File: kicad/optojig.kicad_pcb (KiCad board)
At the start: 2 copper layers, 200 x 100 mm, 20 parts, among them Q1 2N2219, Q2 2N2219, SW1 Switch_SPDT_x2, U1 TRN1-0510, U2 LM358

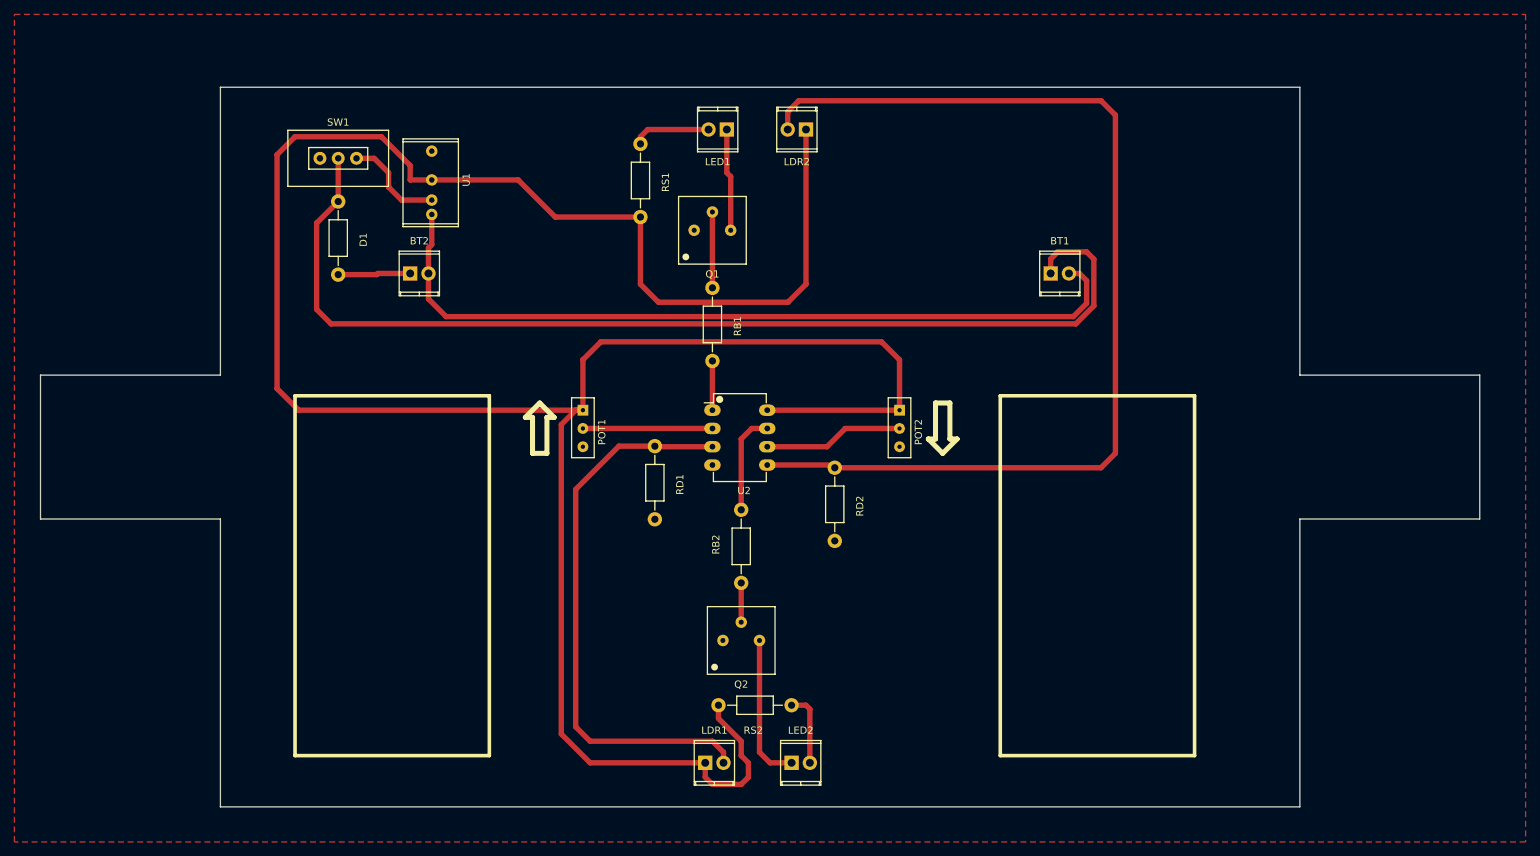
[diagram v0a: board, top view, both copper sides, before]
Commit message: Added battery holder datasheet
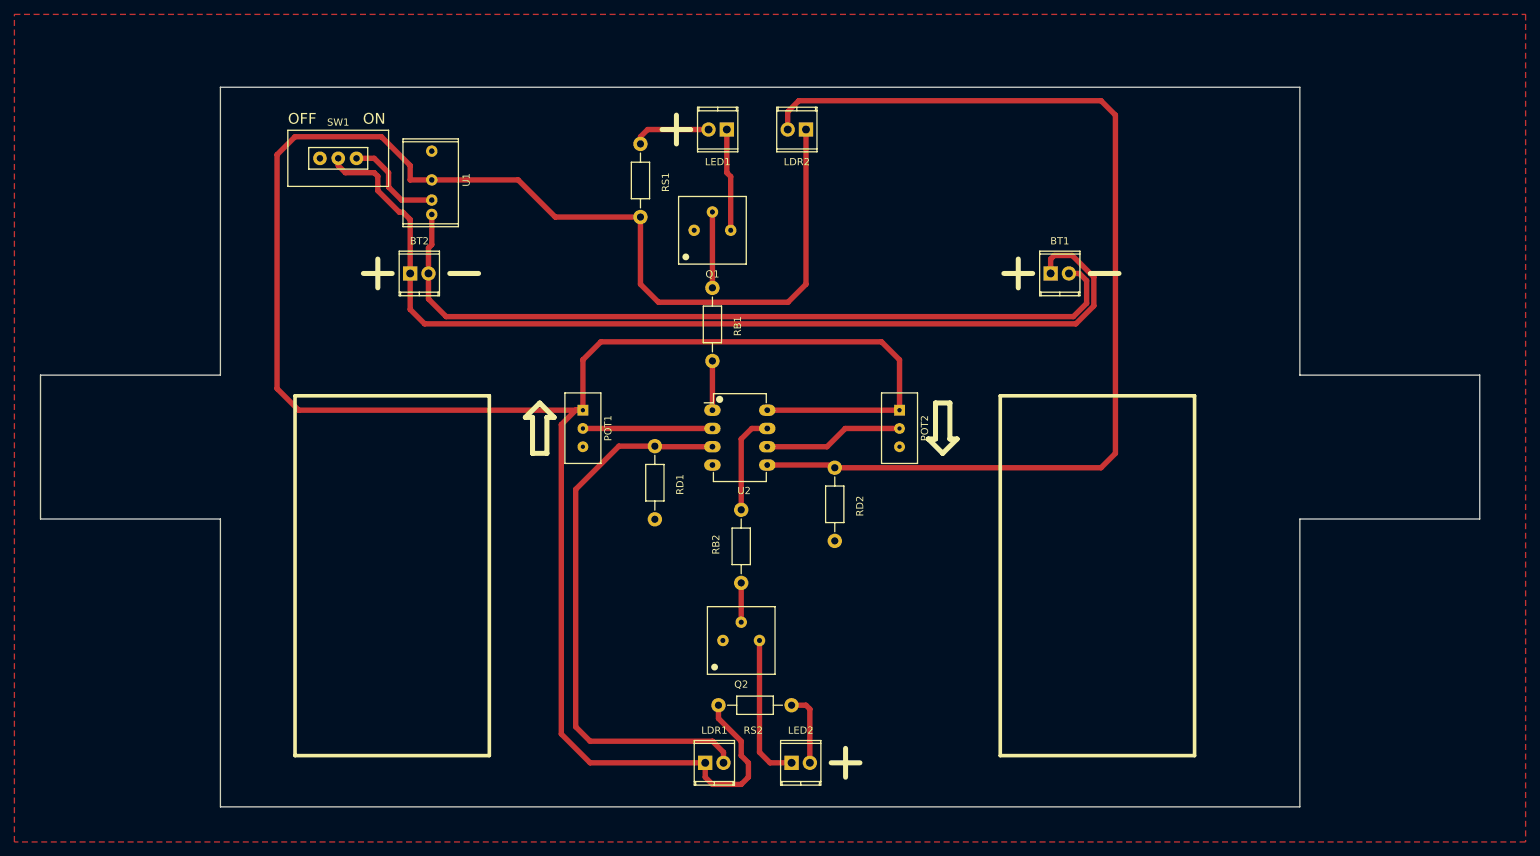
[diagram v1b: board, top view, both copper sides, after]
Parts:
- removed D1: D, Resistors_ThroughHole:Resistor_Horizontal_RM10mm
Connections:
- BT2 pad 1: Net-(BT2-Pad1) -> Net-(BT1-Pad1)
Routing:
- net Net-(BT2-Pad1): track 10.1 -> 0.00 mm
- net Net-(BT1-Pad1): track 147.4 -> 138.1 mm
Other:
- board text added: "OFF"
- board text added: "ON"

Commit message: Added final PCB version
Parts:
- added Battery 1: Batt_hold, optojig-footprints:Batt_hold, F.Cu at (92.8, 115.9)
- added Battery 2: Batt_hold, optojig-footprints:Batt_hold, F.Cu at (190.6, 116.0)
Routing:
- added copper zone on B.Cu, net GND
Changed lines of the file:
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@@
     (area 40 35 250.000001 150.000001)
     (thickness 1.6)
-    (drawings 46)
+    (drawings 38)
     (tracks 109)
     (zones 0)
-    (modules 19)
+    (modules 21)
     (nets 19)
   )
@@
   (layers
     (0 F.Cu signal)
-    (31 B.Cu signal)
-    (32 B.Adhes user)
-    (33 F.Adhes user)
-    (34 B.Paste user)
-    (35 F.Paste user)
-    (36 B.SilkS user)
+    (31 B.Cu signal hide)
+    (32 B.Adhes user hide)
+    (33 F.Adhes user hide)
+    (34 B.Paste user hide)
+    (35 F.Paste user hide)
+    (36 B.SilkS user hide)
     (37 F.SilkS user)
-    (38 B.Mask user)
-    (39 F.Mask user)
-    (40 Dwgs.User user)
-    (41 Cmts.User user)
-    (42 Eco1.User user)
-    (43 Eco2.User user)
-    (44 Edge.Cuts user)
-    (45 Margin user)
-    (46 B.CrtYd user)
-    (47 F.CrtYd user)
-    (48 B.Fab user)
-    (49 F.Fab user)
+    (38 B.Mask user hide)
+    (39 F.Mask user hide)
+    (40 Dwgs.User user hide)
+    (41 Cmts.User user hide)
+    (42 Eco1.User user hide)
+    (43 Eco2.User user hide)
+    (44 Edge.Cuts user hide)
+    (45 Margin user hide)
+    (46 B.CrtYd user hide)
+    (47 F.CrtYd user hide)
+    (48 B.Fab user hide)
+    (49 F.Fab user hide)
   )
   (setup
@@
     (visible_elements FFFFFF7F)
     (pcbplotparams
-      (layerselection 0x00030_80000001)
+      (layerselection 0x010e0_80000001)
       (usegerberextensions false)
       (excludeedgelayer true)
@@
       (outputformat 1)
       (mirror false)
-      (drillshape 1)
+      (drillshape 0)
       (scaleselection 1)
-      (outputdirectory ""))
+      (outputdirectory gerber/))
   )
   (net 0 "")
@@
     (add_net "Net-(SW1-Pad3)")
   )
+  (module optojig-footprints:Batt_hold (layer F.Cu)
+    (at 190.63 115.95)
+    (fp_text reference "Battery 2" (at 0.25 26.05) (layer F.SilkS)
+      (effects (font (size 1 1) (thickness 0.15)))
+    )
+    (fp_text value Batt_hold (at 0 -29) (layer F.Fab)
+      (effects (font (size 1 1) (thickness 0.15)))
+    )
+    (fp_line (start 10 -25) (end 10 -19) (layer F.SilkS) (width 0.7))
+    (fp_line (start 7 -22) (end 13 -22) (layer F.SilkS) (width 0.7))
+    (fp_line (start -15.05 -27.355) (end 15.05 -27.355) (layer F.SilkS) (width 0.7))
+    (fp_line (start -15.05 27.355) (end 15.05 27.355) (layer F.SilkS) (width 0.7))
+    (fp_line (start 15.05 -27.355) (end 15.05 27.355) (layer F.SilkS) (width 0.7))
+    (fp_line (start -15.05 -27.355) (end -15.05 27.355) (layer F.SilkS) (width 0.7))
+    (pad GND thru_hole circle (at -10.98 -13.335) (size 5 5) (drill 2.31) (layers *.Cu *.Mask F.SilkS))
+    (pad GND thru_hole circle (at 10.99 0.455) (size 5 5) (drill 2.31) (layers *.Cu *.Mask F.SilkS))
+    (pad GND thru_hole circle (at -10.98 14.755) (size 5 5) (drill 2.31) (layers *.Cu *.Mask F.SilkS))
+  )
   (module optojig-footprints:TerminalBlock_Buchanan_2way (layer F.Cu)
     (at 184 71)
@@
       (net 6 "Net-(SW1-Pad3)"))
   )
-  (gr_line (start 132 49) (end 132 53) (angle 90) (layer F.SilkS) (width 0.7))
-  (gr_line (start 130 51) (end 134 51) (angle 90) (layer F.SilkS) (width 0.7))
+  (module optojig-footprints:Batt_hold (layer F.Cu)
+    (at 92.75 115.94)
+    (fp_text reference "Battery 1" (at 0.12 25.72) (layer F.SilkS)
+      (effects (font (size 1 1) (thickness 0.15)))
+    )
+    (fp_text value Batt_hold (at 0 -29) (layer F.Fab)
+      (effects (font (size 1 1) (thickness 0.15)))
+    )
+    (fp_line (start 10 -25) (end 10 -19) (layer F.SilkS) (width 0.7))
+    (fp_line (start 7 -22) (end 13 -22) (layer F.SilkS) (width 0.7))
+    (fp_line (start -15.05 -27.355) (end 15.05 -27.355) (layer F.SilkS) (width 0.7))
+    (fp_line (start -15.05 27.355) (end 15.05 27.355) (layer F.SilkS) (width 0.7))
+    (fp_line (start 15.05 -27.355) (end 15.05 27.355) (layer F.SilkS) (width 0.7))
+    (fp_line (start -15.05 -27.355) (end -15.05 27.355) (layer F.SilkS) (width 0.7))
+    (pad GND thru_hole circle (at -10.98 -13.335) (size 5 5) (drill 2.31) (layers *.Cu *.Mask F.SilkS))
+    (pad GND thru_hole circle (at 10.99 0.455) (size 5 5) (drill 2.31) (layers *.Cu *.Mask F.SilkS))
+    (pad GND thru_hole circle (at -10.98 14.755) (size 5 5) (drill 2.31) (layers *.Cu *.Mask F.SilkS))
+  )
+  (gr_line (start 131.5 48.5) (end 131.5 52.5) (angle 90) (layer F.SilkS) (width 0.7))
+  (gr_line (start 129.5 50.5) (end 133.5 50.5) (angle 90) (layer F.SilkS) (width 0.7))
   (gr_line (start 155.5 137) (end 155.5 141) (angle 90) (layer F.SilkS) (width 0.7))
   (gr_line (start 153.5 139) (end 157.5 139) (angle 90) (layer F.SilkS) (width 0.7))
@@
   (gr_line (start 114 96) (end 114 91) (angle 90) (layer F.SilkS) (width 0.7))
   (gr_line (start 112 96) (end 114 96) (angle 90) (layer F.SilkS) (width 0.7))
-  (gr_line (start 79 88) (end 106 88) (angle 90) (layer F.SilkS) (width 0.5))
-  (gr_line (start 79 138) (end 106 138) (angle 90) (layer F.SilkS) (width 0.5))
-  (gr_line (start 79 88) (end 79 138) (angle 90) (layer F.SilkS) (width 0.5))
-  (gr_line (start 106 138) (end 106 88) (angle 90) (layer F.SilkS) (width 0.5))
-  (gr_line (start 204 138) (end 204 88) (angle 90) (layer F.SilkS) (width 0.5))
-  (gr_line (start 177 88) (end 177 138) (angle 90) (layer F.SilkS) (width 0.5))
-  (gr_line (start 177 138) (end 204 138) (angle 90) (layer F.SilkS) (width 0.5))
-  (gr_line (start 177 88) (end 204 88) (angle 90) (layer F.SilkS) (width 0.5))
   (gr_line (start 68.6286 85.1239) (end 68.6286 45.1239) (layer Edge.Cuts) (width 0.1))
   (gr_line (start 43.6286 85.1239) (end 68.6286 85.1239) (layer Edge.Cuts) (width 0.1))
@@
   (segment (start 137 95.08) (end 129.08 95.08) (width 0.75) (layer F.Cu) (net 8))
   (segment (start 129.08 95.08) (end 129 95) (width 0.75) (layer F.Cu) (net 8))
+  (segment (start 163 90) (end 144.62 90) (width 0.75) (layer F.Cu) (net 9))
   (segment (start 98 58) (end 95 58) (width 0.75) (layer F.Cu) (net 9))
   (segment (start 79.5 90) (end 119 90) (width 0.75) (layer F.Cu) (net 9))
@@
   (segment (start 115.16 63.16) (end 127 63.16) (width 0.75) (layer F.Cu) (net 9))
   (segment (start 110 58) (end 115.16 63.16) (width 0.75) (layer F.Cu) (net 9))
-  (segment (start 163 90) (end 144.62 90) (width 0.75) (layer F.Cu) (net 9))
   (segment (start 154 98) (end 191 98) (width 0.75) (layer F.Cu) (net 10))
   (segment (start 147.46 48.54) (end 147.46 51) (width 0.75) (layer F.Cu) (net 10))
@@
   (segment (start 193 96) (end 193 49) (width 0.75) (layer F.Cu) (net 10))
   (segment (start 191 98) (end 193 96) (width 0.75) (layer F.Cu) (net 10))
+  (segment (start 153.62 97.62) (end 154 98) (width 0.75) (layer F.Cu) (net 10))
   (segment (start 144.62 97.62) (end 153.62 97.62) (width 0.75) (layer F.Cu) (net 10))
-  (segment (start 153.62 97.62) (end 154 98) (width 0.75) (layer F.Cu) (net 10))
   (segment (start 136.46 51) (end 128 51) (width 0.75) (layer F.Cu) (net 11))
   (segment (start 127 52) (end 127 53) (width 0.75) (layer F.Cu) (net 11))
@@
   (segment (start 143.54 137.54) (end 145 139) (width 0.75) (layer F.Cu) (net 14))
   (segment (start 137 92.54) (end 119 92.54) (width 0.75) (layer F.Cu) (net 15))
+  (segment (start 152.92 95.08) (end 144.62 95.08) (width 0.75) (layer F.Cu) (net 16))
   (segment (start 163 92.54) (end 155.46 92.54) (width 0.75) (layer F.Cu) (net 16))
-  (segment (start 152.92 95.08) (end 144.62 95.08) (width 0.75) (layer F.Cu) (net 16))
   (segment (start 155.46 92.54) (end 152.92 95.08) (width 0.75) (layer F.Cu) (net 16))
   (segment (start 137 83.16) (end 137 90) (width 0.75) (layer F.Cu) (net 17))
+  (segment (start 142.46 92.54) (end 144.62 92.54) (width 0.75) (layer F.Cu) (net 18))
   (segment (start 141 103.84) (end 141 94) (width 0.75) (layer F.Cu) (net 18))
-  (segment (start 142.46 92.54) (end 144.62 92.54) (width 0.75) (layer F.Cu) (net 18))
   (segment (start 141 94) (end 142.46 92.54) (width 0.75) (layer F.Cu) (net 18))
   (zone (net 7) (net_name GND) (layer F.Cu) (hatch edge 0.508)
     (connect_pads (clearance 0.25))
     (min_thickness 0.254)
+    (fill yes (arc_segments 16) (thermal_gap 0.508) (thermal_bridge_width 3))
+    (polygon
+      (pts
+        (xy 250 150) (xy 40 150) (xy 40 35) (xy 250 35) (xy 250 150)
+      )
+    )
+  )
+  (zone (net 7) (net_name GND) (layer B.Cu) (hatch edge 0.508)
+    (connect_pads (clearance 0.25))
+    (min_thickness 0.254)
